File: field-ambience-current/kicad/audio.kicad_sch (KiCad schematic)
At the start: 29 parts, among them J6 Speaker L (Same Sky CMS-40281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, J7 Speaker R (Same Sky CMS-40281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, J8 3.5mm TRS Line/Headphone Out 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, U3 PCM5102A I²S DAC (TSSOP-20), U4 PAM8403H Class-D Stereo Amp (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

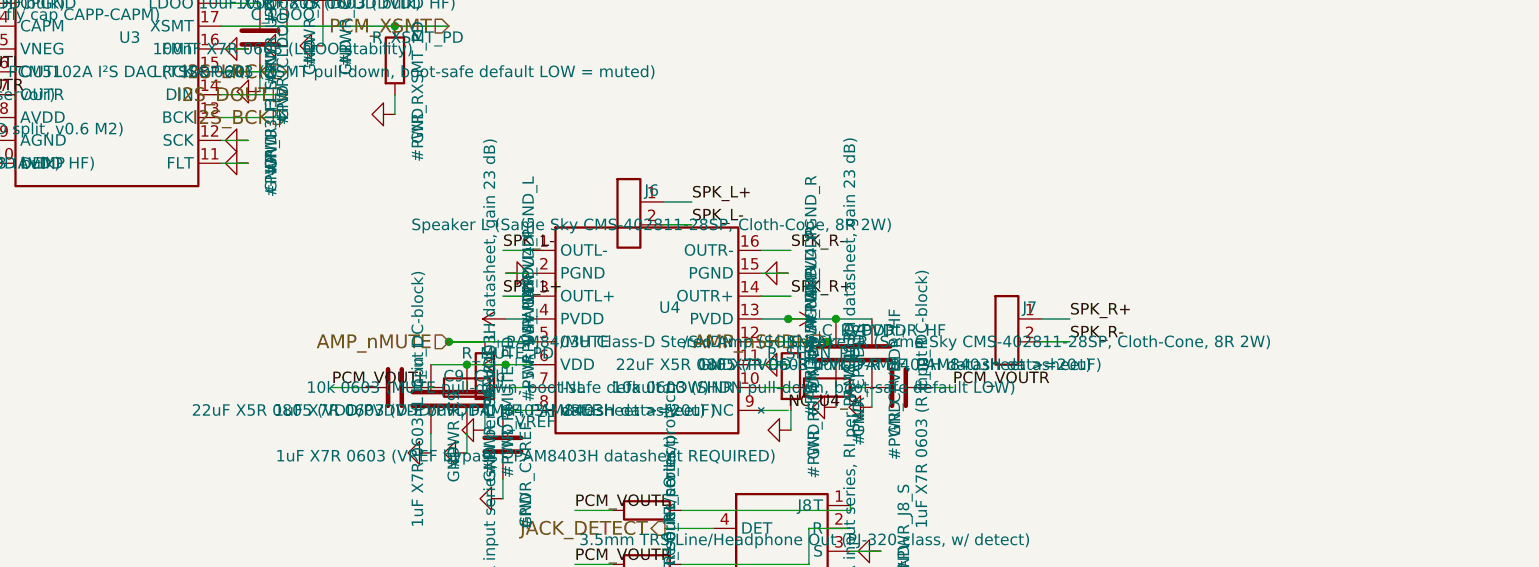
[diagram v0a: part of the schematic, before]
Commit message: audit: fix J3/J6/J7 LCSC doc-drift; flag H743 firmware cell-read gap (r18.76)
User asked to check for any BOM or device-functionality issues. Ran a
systematic audit:

BOM checks:
- No duplicate reference designators across all 201 placed instances
  (verified against the schematic's actual instance paths, not the
  per-sheet symbol-library templates which share generic single-letter
  placeholder refs by design).
- jlc_bom.csv parses cleanly despite several part descriptions containing
  embedded commas (properly CSV-quoted).
- Generator output verified deterministic across repeated runs.

Found and fixed a real doc<->generator drift: the generator had placeholder
"TBD" text in the LCSC field for J3 (LCD module header) and J6/J7 (speaker
headers), even though BOM_MASTER.md already documented the real, correct
codes for these on-board pin headers (C124383 for J3, C124375 for J6/J7) --
the docs had been updated at some point but the generator itself never was.
Synced the generator to use the already-verified codes; jlc_bom.csv now has
zero remaining placeholder LCSC values except the one legitimate case (J4
Tag-Connect, a genuine vendor-direct part with no LCSC listing, already
audited in BOM_MASTER's r18.37 entry).

Functionality check (found, NOT fixed -- flagging only, this session stays
hardware-only per prior PRs):
- src/hal_h743/main_h743.c (the actual STM32H743 product target) still has
  a commented-out TODO stub describing the retired analog Hall-ADC cell-read
  path (adc_read_norm), which has had no signal source since r18.73 moved
  cells to digital MCP23017 GPIO buttons. If implemented literally as
  written, cells would not function on real hardware.
- src/hal_pico/main_pico.c (the bench target) already has a correct, tested
  implementation: it reads cell presses as MCP23017 GPIO edges directly
  (mirroring the modifier-button code two lines above it in the same main
  loop) and calls engine_note_on/off, bypassing the old velocity state
  machine entirel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
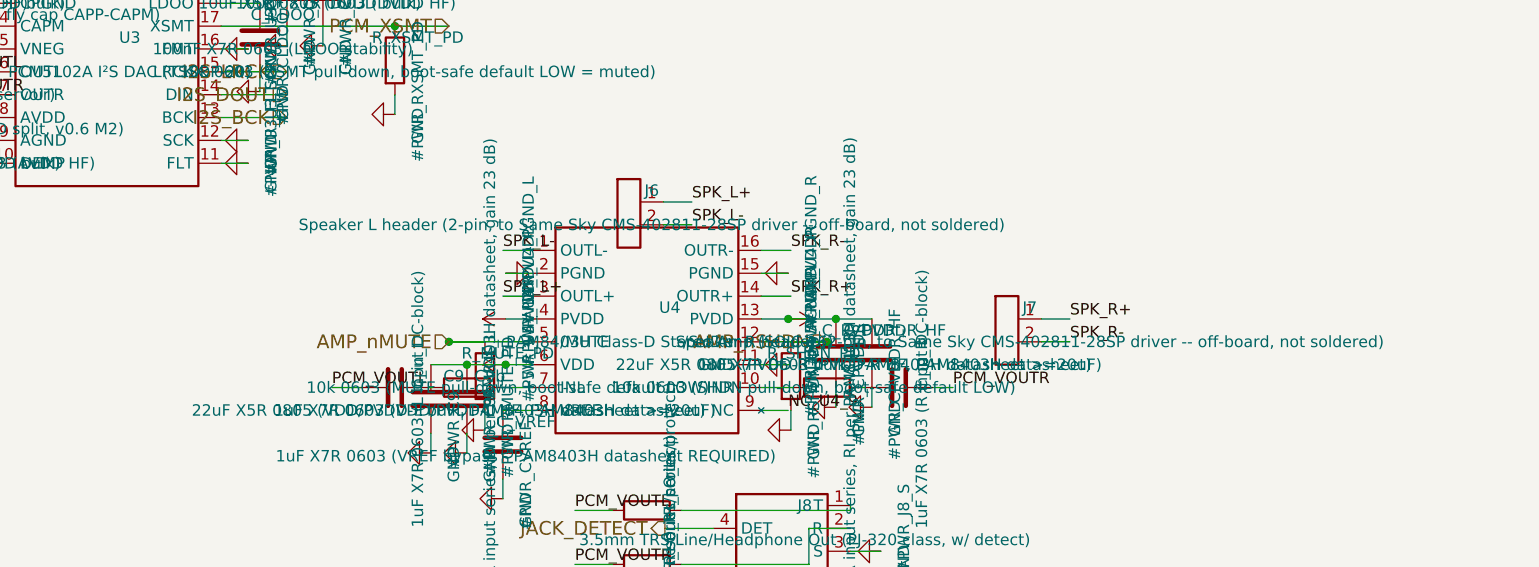
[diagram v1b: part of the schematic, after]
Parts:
- J6: value Speaker L (Same Sky CMS-402811-28SP, Cloth-Cone, 8R 2W) -> Speaker L header (2-pin, to Same Sky CMS-402811-28SP driver -- off-board, not soldered); LCSC TBD (kein LCSC-Stock fuer 40mm-Treiber; DigiKey 102-CMS-402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 -> C124375; MPN Same Sky CMS-402811-28SP (Cloth-Cone primaer; PUI AS04008PS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 -> 1x2 2.54mm pin header (the on-board connector); Notes Treiber haengt vom Top-Panel (Top-Firing, ADR-0007/ADR-0011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 -> Treiber (Same Sky CMS-402811-28SP, Cloth-Cone primaer; PUI 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
- J7: value Speaker R (Same Sky CMS-402811-28SP, Cloth-Cone, 8R 2W) -> Speaker R header (2-pin, to Same Sky CMS-402811-28SP driver -- off-board, not soldered); LCSC TBD (kein LCSC-Stock fuer 40mm-Treiber; DigiKey 102-CMS-402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 -> C124375; MPN Same Sky CMS-402811-28SP (Cloth-Cone primaer; PUI AS04008PS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 -> 1x2 2.54mm pin header (the on-board connector); Notes Treiber haengt vom Top-Panel (Top-Firing, ADR-0007/ADR-0011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 -> Treiber (Same Sky CMS-402811-28SP, Cloth-Cone primaer; PUI 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
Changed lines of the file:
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@@
       (property "Reference" "J6" (at 160.54 114.46 0)
         (effects (font (size 1.27 1.27))))
-      (property "Value" "Speaker L (Same Sky CMS-402811-28SP, Cloth-Cone, 8R 2W)" (at 160.54 118.27 0)
+      (property "Value" "Speaker L header (2-pin, to Same Sky CMS-402811-28SP driver -- off-board, not soldered)" (at 160.54 118.27 0)
         (effects (font (size 1.27 1.27))))
       (property "Footprint" "Connector_PinHeader_2.54mm:PinHeader_1x02_P2.54mm_Vertical" (at 158 117 0)
@@
       (property "Datasheet" "~" (at 158 117 0)
         (effects (font (size 1.27 1.27)) hide))
-      (property "MPN" "Same Sky CMS-402811-28SP (Cloth-Cone primaer; PUI AS04008PS-4W-WR-R sekundaer)" (at 160.54 120.81 0)
+      (property "MPN" "1x2 2.54mm pin header (the on-board connector)" (at 160.54 120.81 0)
         (effects (font (size 1.27 1.27)) hide))
-      (property "LCSC" "TBD (kein LCSC-Stock fuer 40mm-Treiber; DigiKey 102-CMS-402811-28SP-ND)" (at 160.54 122.08 0)
+      (property "LCSC" "C124375" (at 160.54 122.08 0)
         (effects (font (size 1.27 1.27)) hide))
-      (property "Notes" "Treiber haengt vom Top-Panel (Top-Firing, ADR-0007/ADR-0011), kein PCB-Mount. J6/J7 sind nur 2-Pin-Loetpads; Draht zum Treiber-Eyelet manuell. r18.18: Cloth-Cone-Wechsel." (at 160.54 123.35 0)
+      (property "Notes" "Treiber (Same Sky CMS-402811-28SP, Cloth-Cone primaer; PUI AS04008PS-4W-WR-R sekundaer) haengt vom Top-Panel (Top-Firing, ADR-0007/ADR-0011), kein PCB-Mount, kein LCSC-Stock fuer den 40mm-Treiber selbst (DigiKey 102-CMS-402811-28SP-ND). J6/J7 sind nur 2-Pin-Loetpads; Draht zum Treiber-Eyelet manuell. r18.18: Cloth-Cone-Wechsel." (at 160.54 123.35 0)
         (effects (font (size 1.27 1.27)) hide))
     (instances
@@
       (property "Reference" "J7" (at 202.54 127.46 0)
         (effects (font (size 1.27 1.27))))
-      (property "Value" "Speaker R (Same Sky CMS-402811-28SP, Cloth-Cone, 8R 2W)" (at 202.54 131.27 0)
+      (property "Value" "Speaker R header (2-pin, to Same Sky CMS-402811-28SP driver -- off-board, not soldered)" (at 202.54 131.27 0)
         (effects (font (size 1.27 1.27))))
       (property "Footprint" "Connector_PinHeader_2.54mm:PinHeader_1x02_P2.54mm_Vertical" (at 200 130 0)
@@
       (property "Datasheet" "~" (at 200 130 0)
         (effects (font (size 1.27 1.27)) hide))
-      (property "MPN" "Same Sky CMS-402811-28SP (Cloth-Cone primaer; PUI AS04008PS-4W-WR-R sekundaer)" (at 202.54 133.81 0)
+      (property "MPN" "1x2 2.54mm pin header (the on-board connector)" (at 202.54 133.81 0)
         (effects (font (size 1.27 1.27)) hide))
-      (property "LCSC" "TBD (kein LCSC-Stock fuer 40mm-Treiber; DigiKey 102-CMS-402811-28SP-ND)" (at 202.54 135.08 0)
+      (property "LCSC" "C124375" (at 202.54 135.08 0)
         (effects (font (size 1.27 1.27)) hide))
-      (property "Notes" "Treiber haengt vom Top-Panel (Top-Firing, ADR-0007/ADR-0011), kein PCB-Mount. J6/J7 sind nur 2-Pin-Loetpads; Draht zum Treiber-Eyelet manuell. r18.18: Cloth-Cone-Wechsel." (at 202.54 136.35 0)
+      (property "Notes" "Treiber (Same Sky CMS-402811-28SP, Cloth-Cone primaer; PUI AS04008PS-4W-WR-R sekundaer) haengt vom Top-Panel (Top-Firing, ADR-0007/ADR-0011), kein PCB-Mount, kein LCSC-Stock fuer den 40mm-Treiber selbst (DigiKey 102-CMS-402811-28SP-ND). J6/J7 sind nur 2-Pin-Loetpads; Draht zum Treiber-Eyelet manuell. r18.18: Cloth-Cone-Wechsel." (at 202.54 136.35 0)
         (effects (font (size 1.27 1.27)) hide))
     (instances
